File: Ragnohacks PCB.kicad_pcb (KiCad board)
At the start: 2 copper layers, 85.6 x 54 mm, 38 parts, among them J1 Conn_01x02, J2 Conn_01x18, J3 Conn_01x18, J4 USB_A, J5 USB_C_Receptacle_USB2.0_16P, SW1 SW_Push, U1 RP2040, U2 W25Q128JVS, U3 LD1117S33TR_SOT223, U4 USBLC6-2P6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

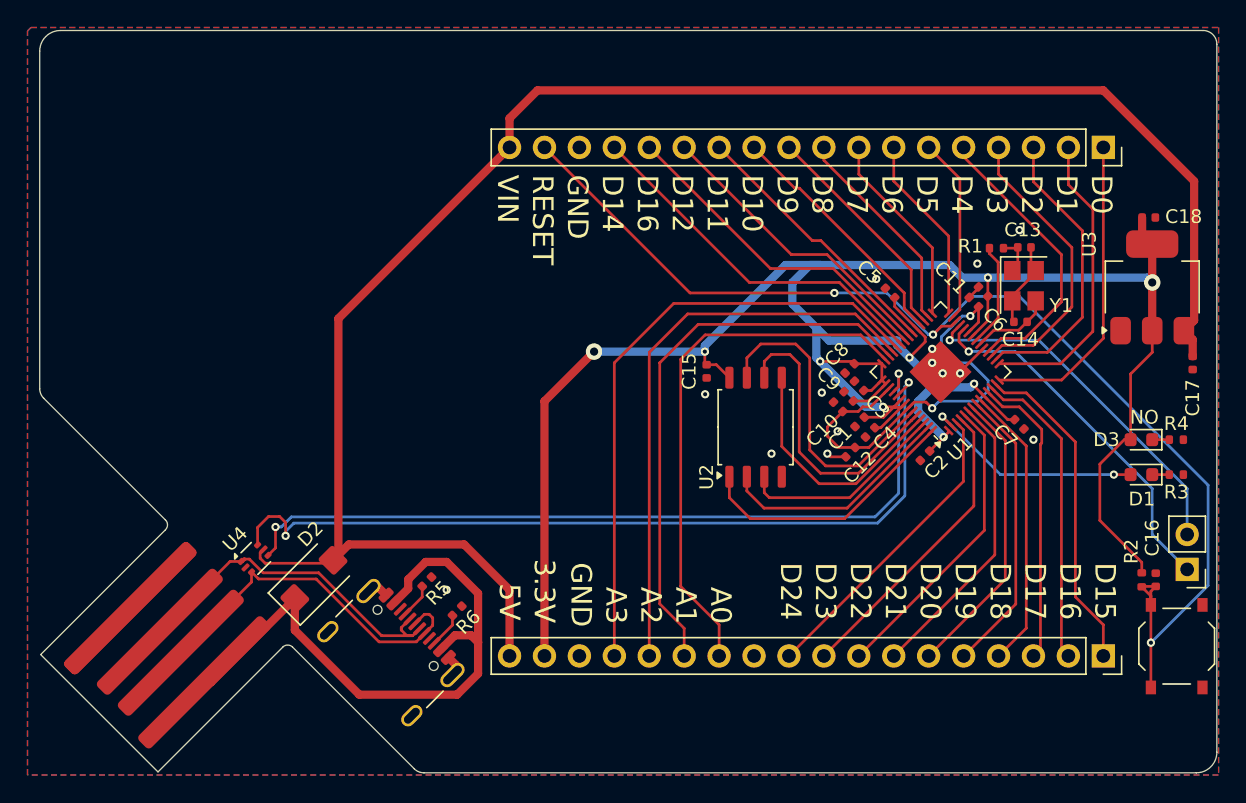
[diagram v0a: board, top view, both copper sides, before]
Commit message: Move USB port, routing adjustments
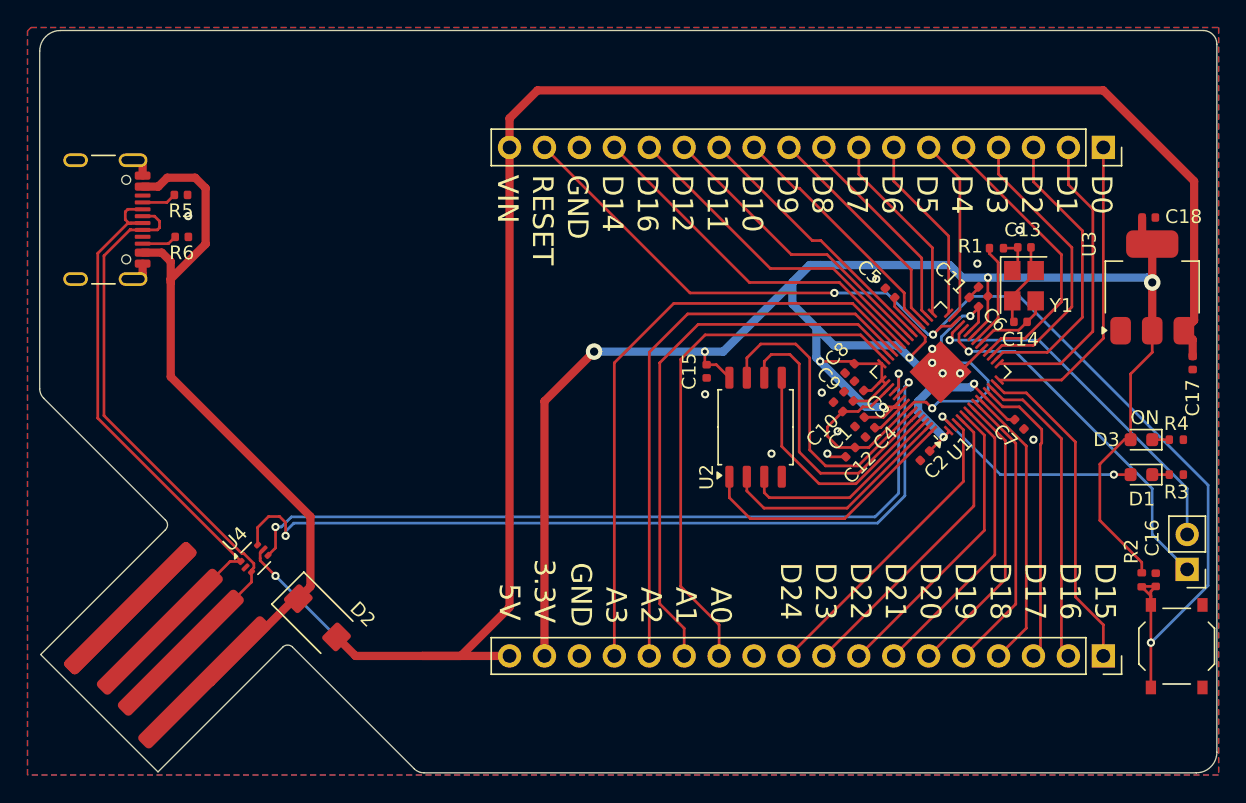
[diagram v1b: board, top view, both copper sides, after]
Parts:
- moved J5 38.5 mm to (102.1, 90.4), turned to -90 degrees
- moved R6 33.8 mm to (108.8, 91.7), turned to 180 degrees
- moved R5 33.3 mm to (108.7, 88.6), turned to 180 degrees
- moved D2 2.81 mm to (118.6, 119.4), turned to -45 degrees
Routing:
- net DP: track 26.0 -> 42.4 mm
- net DN: track 26.0 -> 42.3 mm
- net +5V: track 129.9 -> 145.1 mm, vias 0 -> 1
- net Net-(D2-A): track 45.2 -> 53.6 mm
- net +3V3: track 169.1 -> 167.9 mm
